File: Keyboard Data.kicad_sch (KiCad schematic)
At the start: 4 parts, among them U2 74AHC595, U3 74AHC595, U4 74AHC595, U5 74AHC595

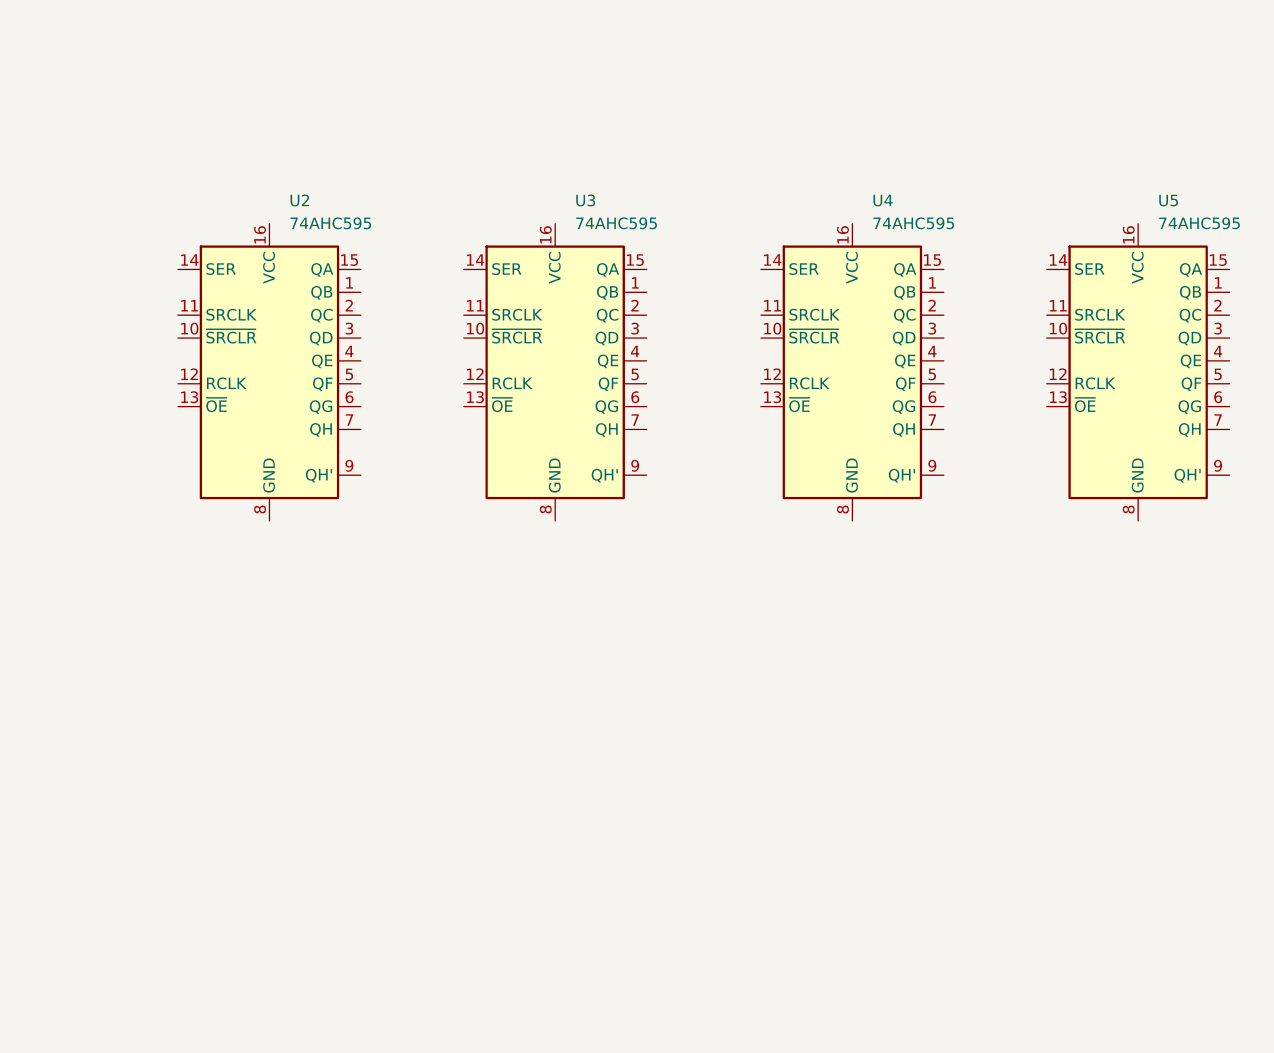
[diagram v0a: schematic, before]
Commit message: Keyboard Data Changes and added footprints
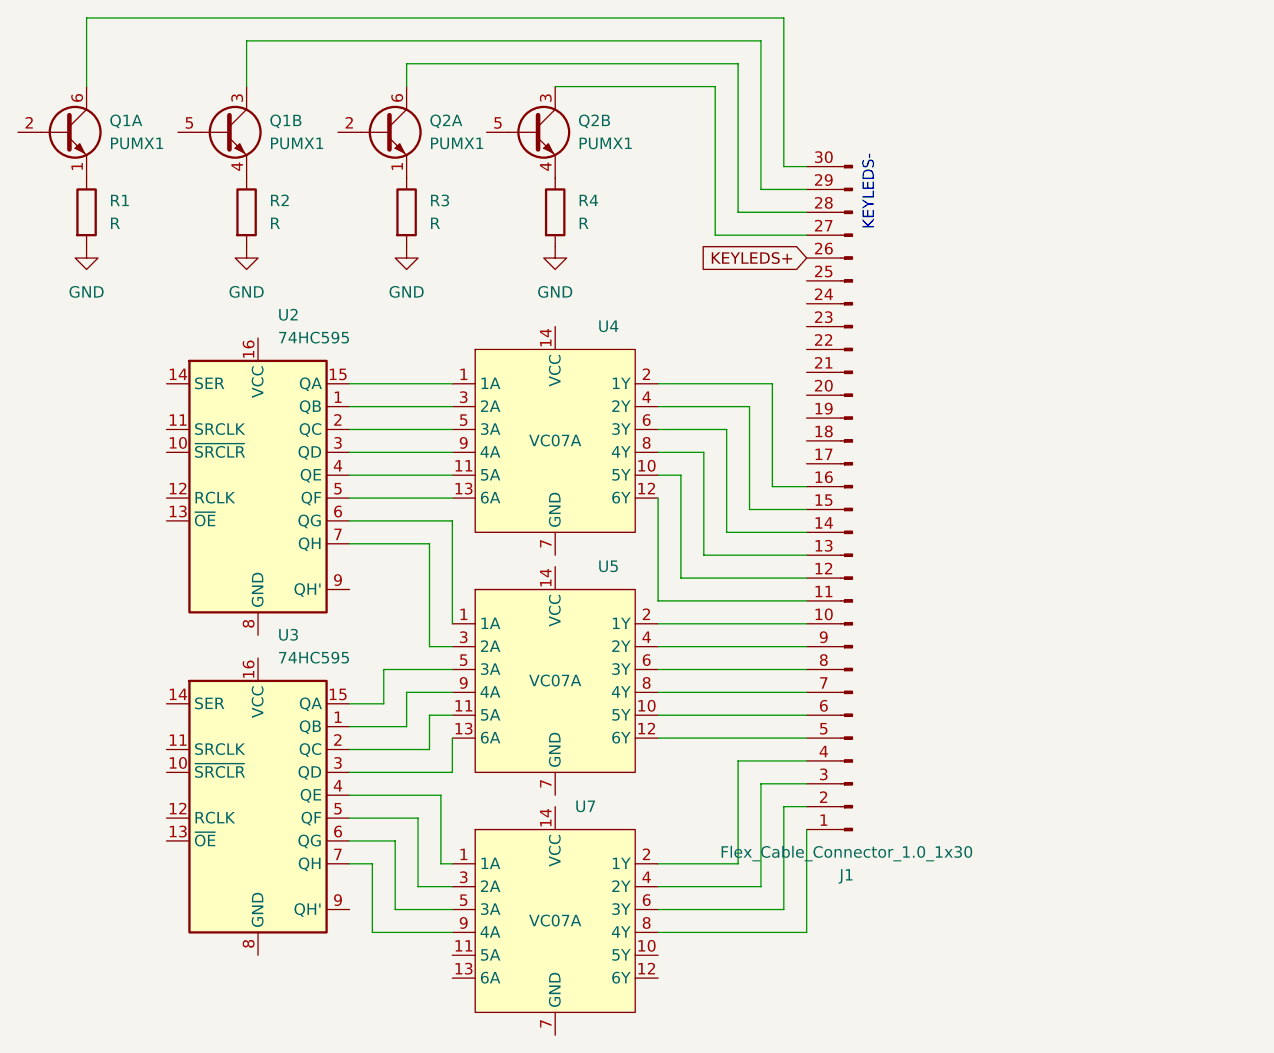
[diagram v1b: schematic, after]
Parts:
- removed U2, U3, U4, U5: 74AHC595, Package_SO:TSSOP-16_4.4x5mm_P0.65mm, symbol 74xx:74AHC595
- added J1: Flex_Cable_Connector_1.0_1x30, Connector_FFC-FPC:Molex_200528-0300_1x30-1MP_P1.00mm_Horizontal, symbol logipcbslib:Flex_Cable_Connector_1.0_1x30
- added Q1, Q2: PUMX1, Package_TO_SOT_SMD:SOT-363_SC-70-6, symbol Transistor_BJT:PUMX1
- added R1, R2, R3, R4: R, Resistor_SMD:R_0603_1608Metric_Pad0.98x0.95mm_HandSolder, symbol Device:R
- added U2, U3: 74HC595, Package_SO:TSSOP-16_4.4x5mm_P0.65mm, symbol 74xx:74HC595
- added U4, U5, U7: VC07A, Package_DFN_QFN:Texas_S-PVQFN-N14, symbol logisch:C07A
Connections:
- new net: U2.6 (QG), U5.1 (1A)
- new net: J1.6 (Pin_6), U5.10 (5Y)
- new net: U3.2 (QC), U5.11 (5A)
- new net: J1.5 (Pin_5), U5.12 (6Y)
- new net: U3.3 (QD), U5.13 (6A)
- new net: J1.10 (Pin_10), U5.2 (1Y)
- new net: U2.7 (QH), U5.3 (2A)
- new net: J1.9 (Pin_9), U5.4 (2Y)
- new net: U3.15 (QA), U5.5 (3A)
- new net: J1.8 (Pin_8), U5.6 (3Y)
- new net: J1.7 (Pin_7), U5.8 (4Y)
- new net: U3.1 (QB), U5.9 (4A)
- new net: J1.27 (Pin_27), Q2.3 (C2)
- new net: Q2.4 (E2), R4.1
- new net: J1.29 (Pin_29), Q1.3 (C2)
- new net: Q1.4 (E2), R2.1
- new net: U2.15 (QA), U4.1 (1A)
- new net: J1.12 (Pin_12), U4.10 (5Y)
- new net: U2.4 (QE), U4.11 (5A)
- new net: J1.11 (Pin_11), U4.12 (6Y)
- new net: U2.5 (QF), U4.13 (6A)
- new net: J1.16 (Pin_16), U4.2 (1Y)
- new net: U2.1 (QB), U4.3 (2A)
- new net: J1.15 (Pin_15), U4.4 (2Y)
- new net: U2.2 (QC), U4.5 (3A)
- new net: J1.14 (Pin_14), U4.6 (3Y)
- new net: J1.13 (Pin_13), U4.8 (4Y)
- new net: U2.3 (QD), U4.9 (4A)
- new net: U3.4 (QE), U7.1 (1A)
- new net: J1.4 (Pin_4), U7.2 (1Y)
- new net: U3.5 (QF), U7.3 (2A)
- new net: J1.3 (Pin_3), U7.4 (2Y)
- new net: U3.6 (QG), U7.5 (3A)
- new net: J1.2 (Pin_2), U7.6 (3Y)
- new net: J1.1 (Pin_1), U7.8 (4Y)
- new net: U3.7 (QH), U7.9 (4A)
- new net: Q1.1 (E1), R1.1
- new net: J1.30 (Pin_30), Q1.6 (C1)
- new net: Q2.1 (E1), R3.1
- new net: J1.28 (Pin_28), Q2.6 (C1)
- new net GND: R1.2, R2.2, R3.2, R4.2
- new net KEYLEDS+: J1.26 (Pin_26)
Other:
- note added: "KEYLEDS-"

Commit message: Atmega34u4
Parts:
- U4, U5, U7: footprint Package_DFN_QFN:Texas_S-PVQFN-N14 -> Package_SO:TSSOP-14_4.4x5mm_P0.65mm
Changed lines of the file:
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@@
 			)
 		)
-		(property "Footprint" "Package_DFN_QFN:Texas_S-PVQFN-N14"
+		(property "Footprint" "Package_SO:TSSOP-14_4.4x5mm_P0.65mm"
 			(at 111.76 113.03 0)
 			(effects
@@
 			)
 		)
-		(property "Footprint" "Package_DFN_QFN:Texas_S-PVQFN-N14"
+		(property "Footprint" "Package_SO:TSSOP-14_4.4x5mm_P0.65mm"
 			(at 111.76 86.36 0)
 			(effects
@@
 			)
 		)
-		(property "Footprint" "Package_DFN_QFN:Texas_S-PVQFN-N14"
+		(property "Footprint" "Package_SO:TSSOP-14_4.4x5mm_P0.65mm"
 			(at 111.76 139.7 0)
 			(effects
